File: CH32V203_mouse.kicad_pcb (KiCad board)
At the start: 4 copper layers, 30 parts, among them J1 USB_C_Receptacle_USB2.0_16P_u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, J2 Conn_01x05_Pin, J3 Conn_01x04_Pin, SW1 SW_Push, U1 CH32V203G6U6, U2 USBLC6-2SC6, U3 XC6206P332MR, X1 16MHz

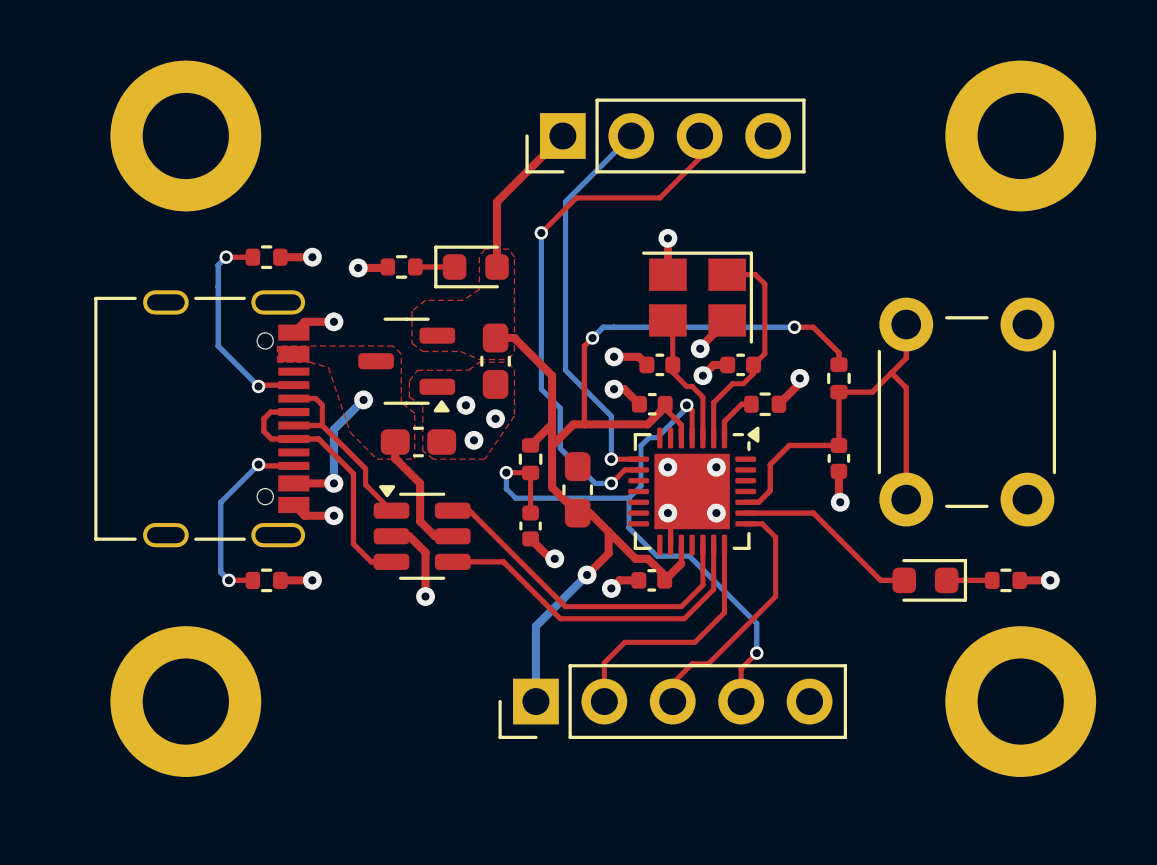
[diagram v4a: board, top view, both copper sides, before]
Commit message: Board outline set missing 3D files added
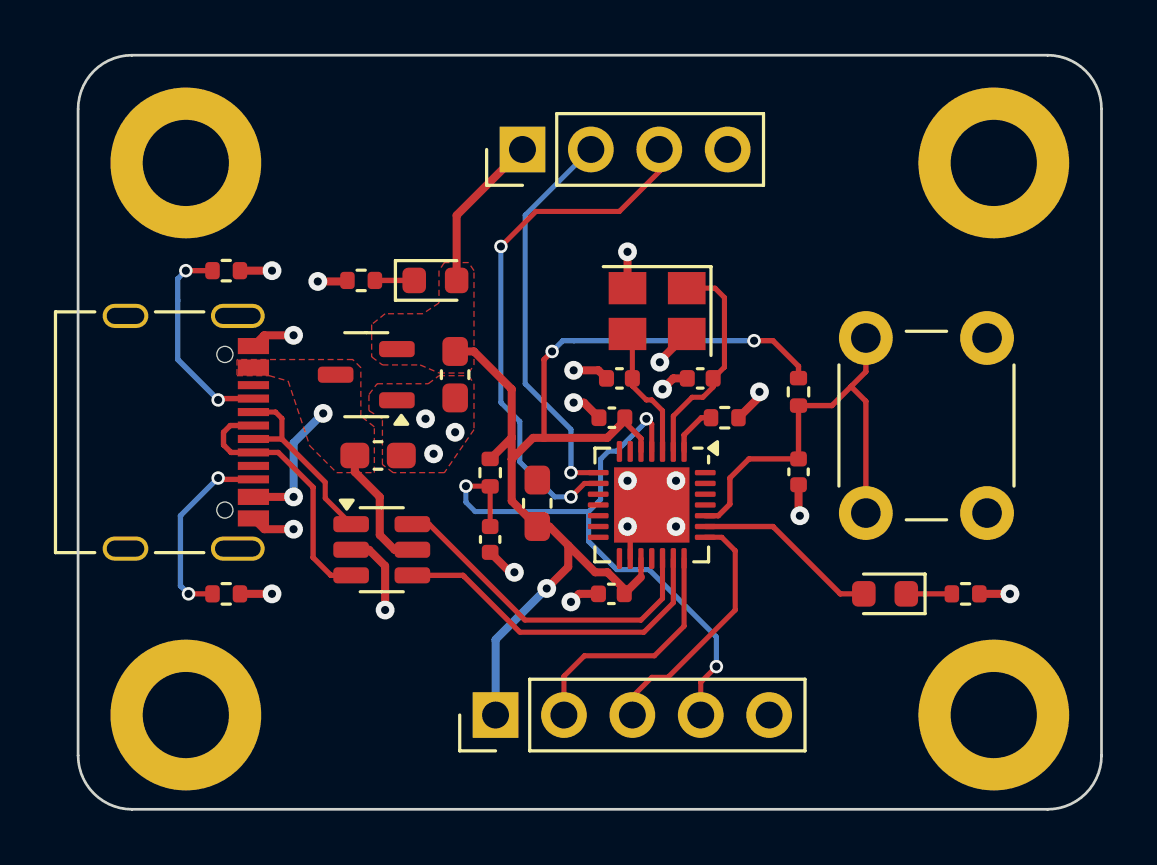
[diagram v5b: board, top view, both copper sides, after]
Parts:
- moved C1 1.58 mm to (129.1, 98.9)
- moved C2 1.58 mm to (132.0, 95.9)
- moved C3 1.58 mm to (135.1, 100.6)
- moved C4 1.58 mm to (137.8, 97.5)
- moved C5 1.58 mm to (137.8, 104.0)
- moved C6 1.58 mm to (141.1, 96.0)
- moved C7 1.58 mm to (138.1, 96.0)
- moved C8 1.58 mm to (144.8, 99.5)
- moved C9 1.58 mm to (133.3, 102.0)
- moved D1 1.58 mm to (131.3, 92.4)
- moved D2 1.58 mm to (148.0, 104.0)
- moved J1 1.58 mm to (122.0, 98.0)
- moved J2 1.58 mm to (133.5, 108.5)
- moved J3 1.58 mm to (134.5, 87.5)
- moved R1 1.58 mm to (123.5, 92.0)
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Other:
- board outline added: 38 x 28 mm

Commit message: GND pours on inner layers fixed DRC violations
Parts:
- moved C9 0.06 mm to (133.4, 102.0)
- moved C1 0.06 mm to (129.2, 98.8)
- moved C2 0.06 mm to (132.1, 95.8)
- moved C3 0.06 mm to (135.1, 100.6)
- moved C4 0.06 mm to (137.9, 97.4)
- moved C5 0.06 mm to (137.9, 104.0)
- moved C6 0.06 mm to (141.2, 96.0)
- moved C7 0.06 mm to (138.2, 96.0)
- moved C8 0.06 mm to (144.8, 99.5)
- moved D2 0.06 mm to (148.0, 104.0)
- moved J1 0.06 mm to (122.1, 98.0)
- moved J2 0.06 mm to (133.6, 108.5)
- moved J3 0.06 mm to (134.6, 87.5)
- moved R1 0.06 mm to (123.6, 92.0)
- moved R2 0.06 mm to (123.6, 104.0)
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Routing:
- net GND: track 24.6 -> 26.1 mm, vias 23 -> 24
- added copper zone on In1.Cu, net GND
- added copper zone on In2.Cu, net GND

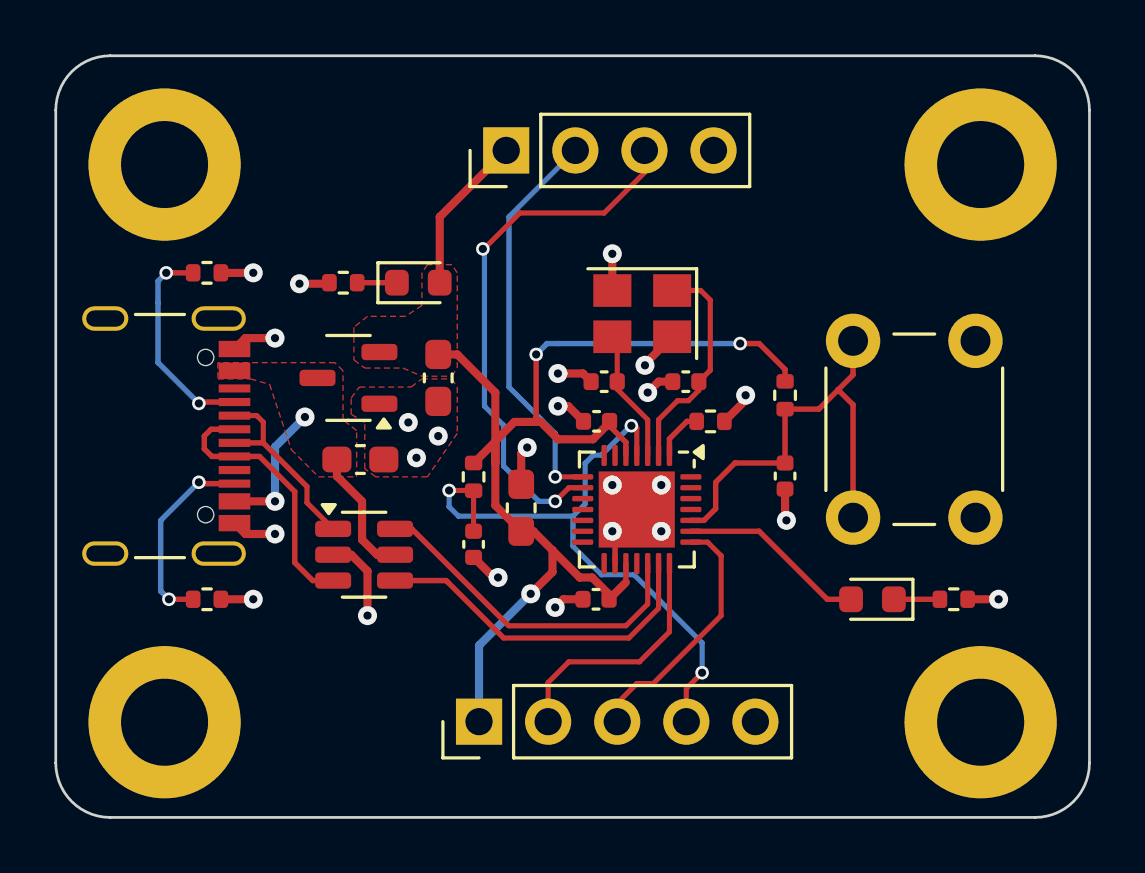
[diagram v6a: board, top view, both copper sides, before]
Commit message: Shifted all components so USB connector overhangs correctly
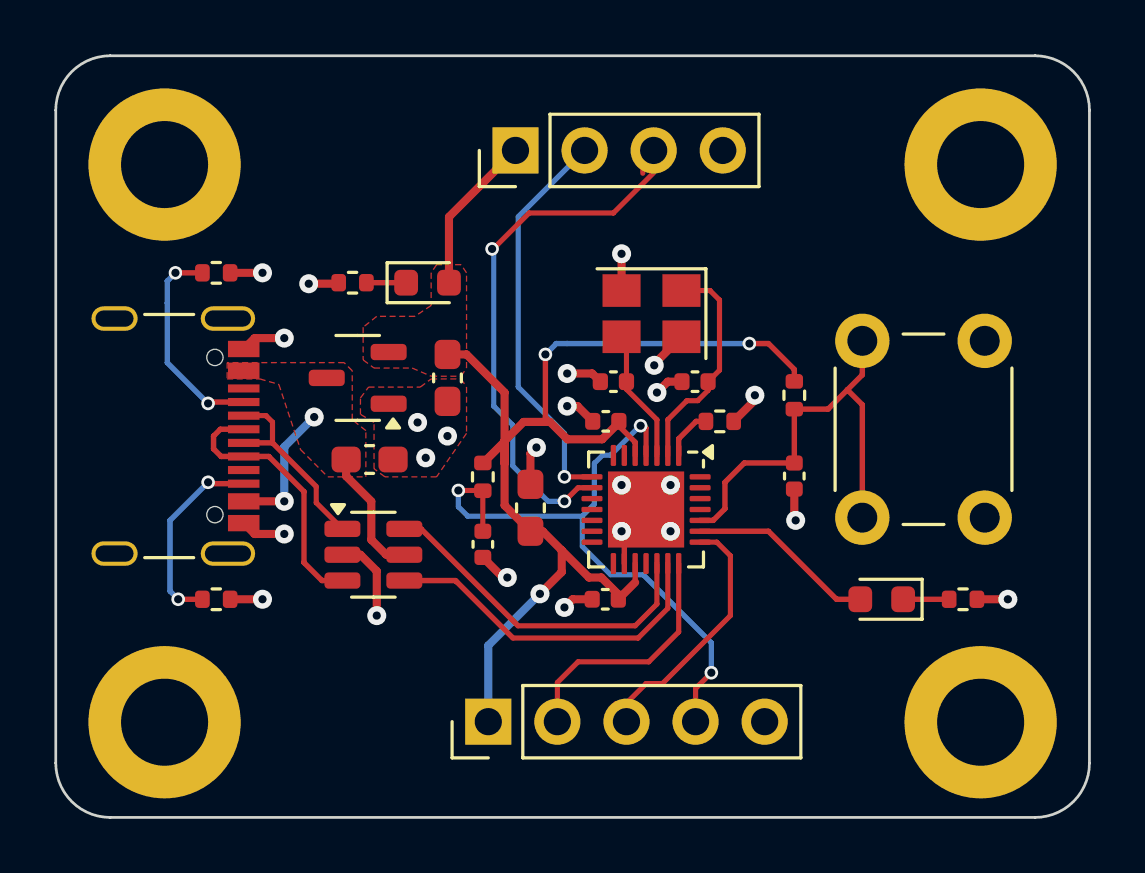
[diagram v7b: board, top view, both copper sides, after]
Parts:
- moved C1 0.34 mm to (129.5, 98.8)
- moved C2 0.34 mm to (132.4, 95.8)
- moved C4 0.34 mm to (138.2, 97.4)
- moved C6 0.34 mm to (141.5, 96.0)
- moved C7 0.34 mm to (138.5, 96.0)
- moved C8 0.34 mm to (145.2, 99.5)
- moved D1 0.34 mm to (131.7, 92.3)
- moved D2 0.34 mm to (148.4, 104.0)
- moved J1 0.34 mm to (122.4, 98.0)
- moved J2 0.34 mm to (133.9, 108.5)
- moved J3 0.34 mm to (134.9, 87.5)
- moved R1 0.34 mm to (123.9, 92.0)
- moved R2 0.34 mm to (123.9, 104.0)
- moved R3 0.34 mm to (128.9, 92.3)
- moved R4 0.34 mm to (151.4, 104.0)
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
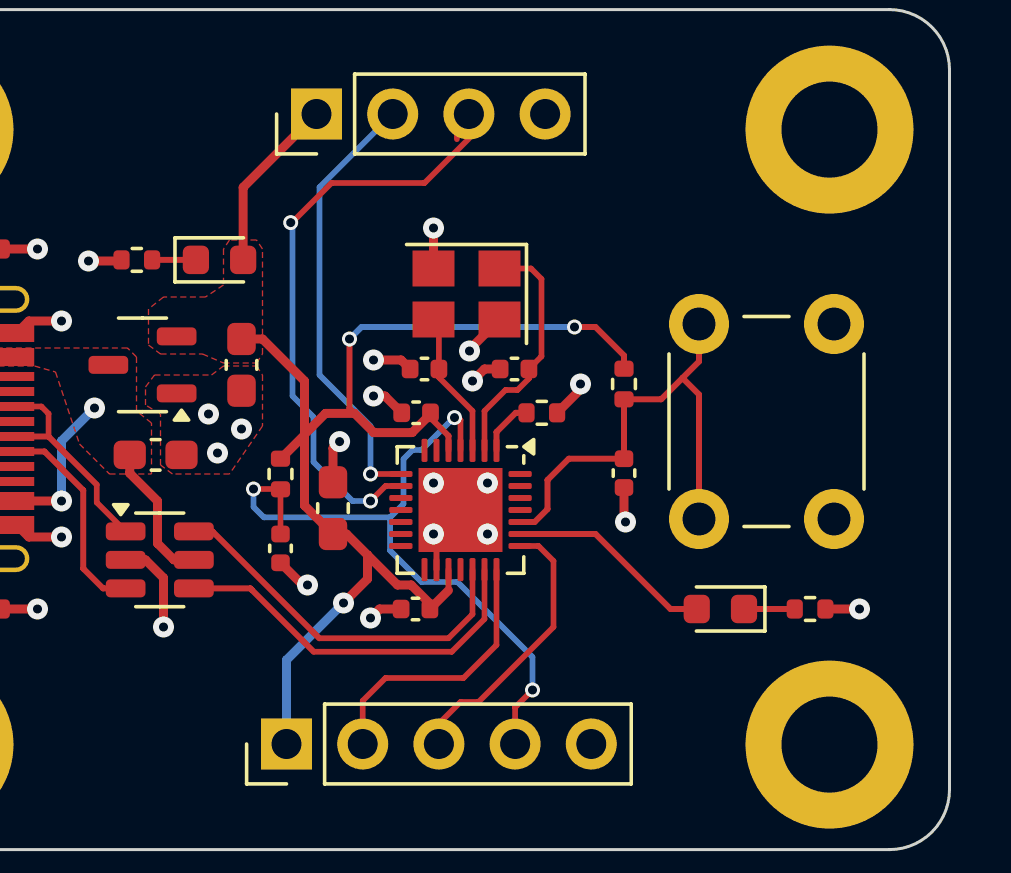
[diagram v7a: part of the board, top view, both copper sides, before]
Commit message: Bare copper points for BOOT0 and NRST BOOT0 resistor relocated silkscreen added
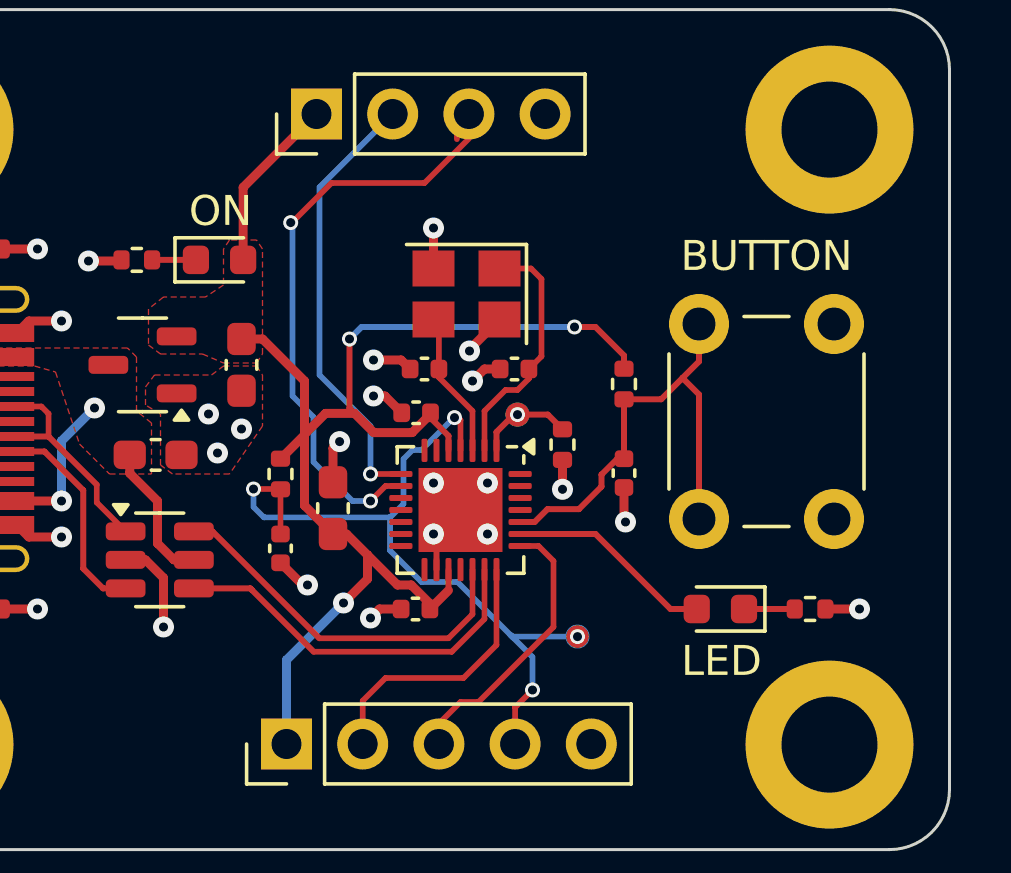
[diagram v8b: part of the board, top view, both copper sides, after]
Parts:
- moved R7 1.26 mm to (143.1, 98.5), turned to 90 degrees
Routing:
- net /NRST: track 24.0 -> 26.4 mm, vias 3 -> 4
- net /BOOT0: track 1.88 -> 3.44 mm, vias 0 -> 1
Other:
- board text added: "3V3"
- board text added: "BOOT0"
- board text added: "BUTTON"
- board text added: "CH32V203 mouse"
- board text added: "GND"
- board text added: "LED"
- board text added: "NRST"
- board text added: "ON"
- board text added: "RX"
- board text added: "SWCLK"
- board text added: "SWDIO"
- board text added: "TX"
- board text added: "github.com/m-fudala"
